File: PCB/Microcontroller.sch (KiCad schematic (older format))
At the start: 9 parts

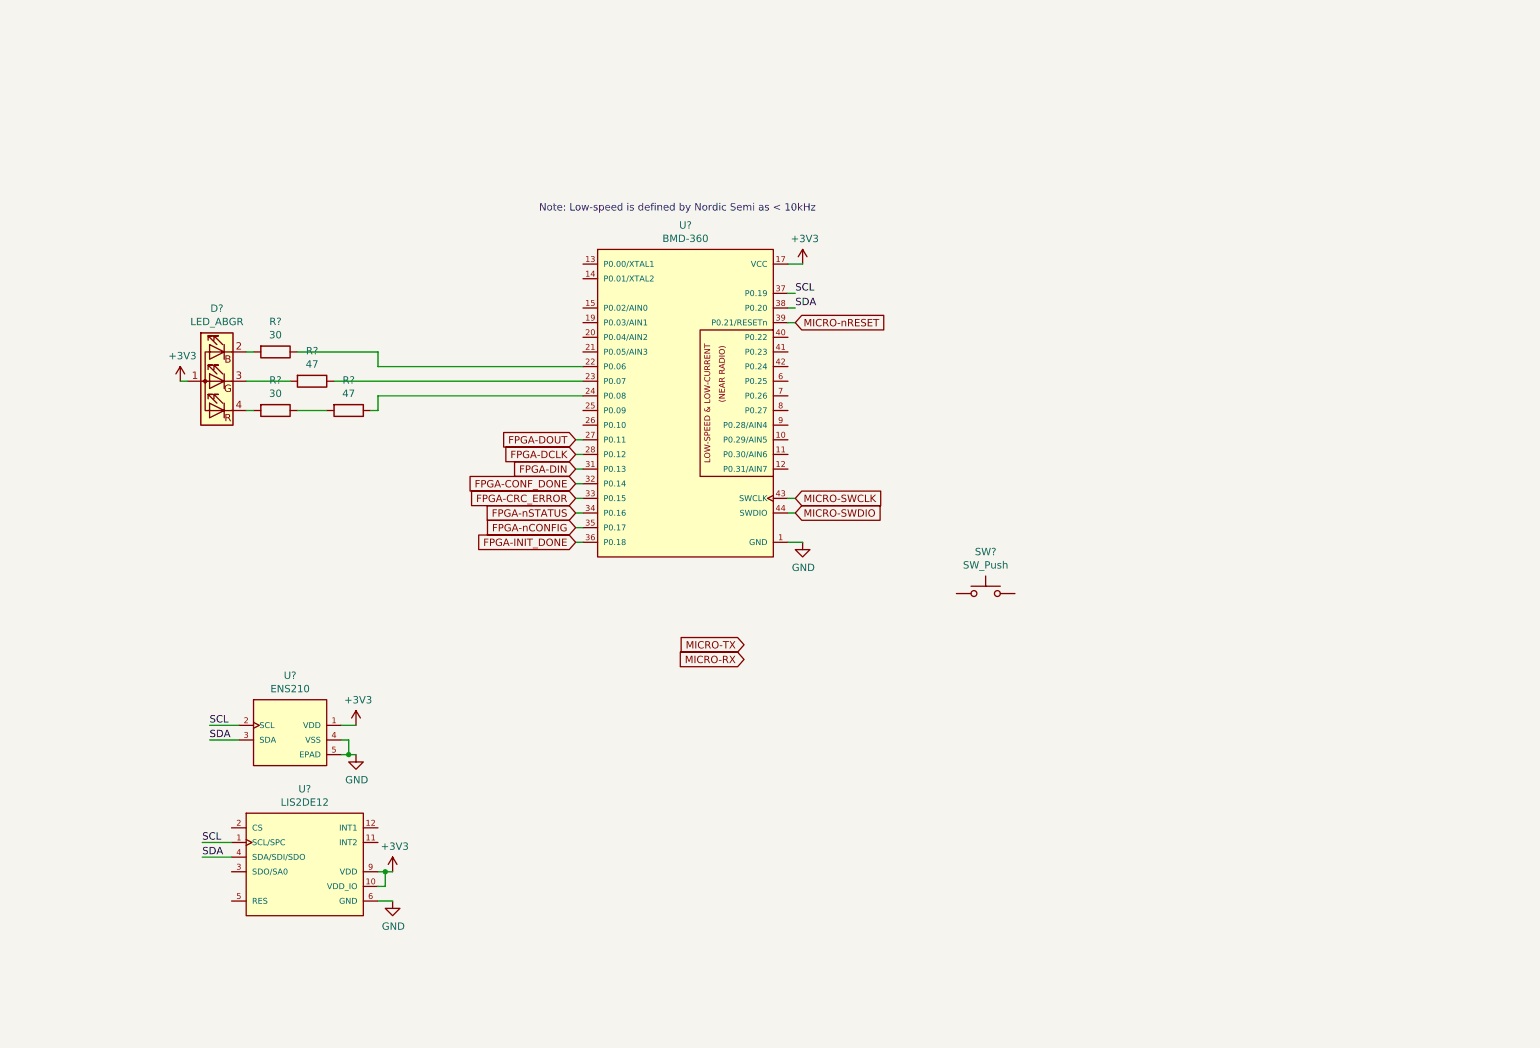
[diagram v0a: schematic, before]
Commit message: Connect push buttons to microcontroller, connect I2C lines, add GPIO links between microcontroller and FPGA
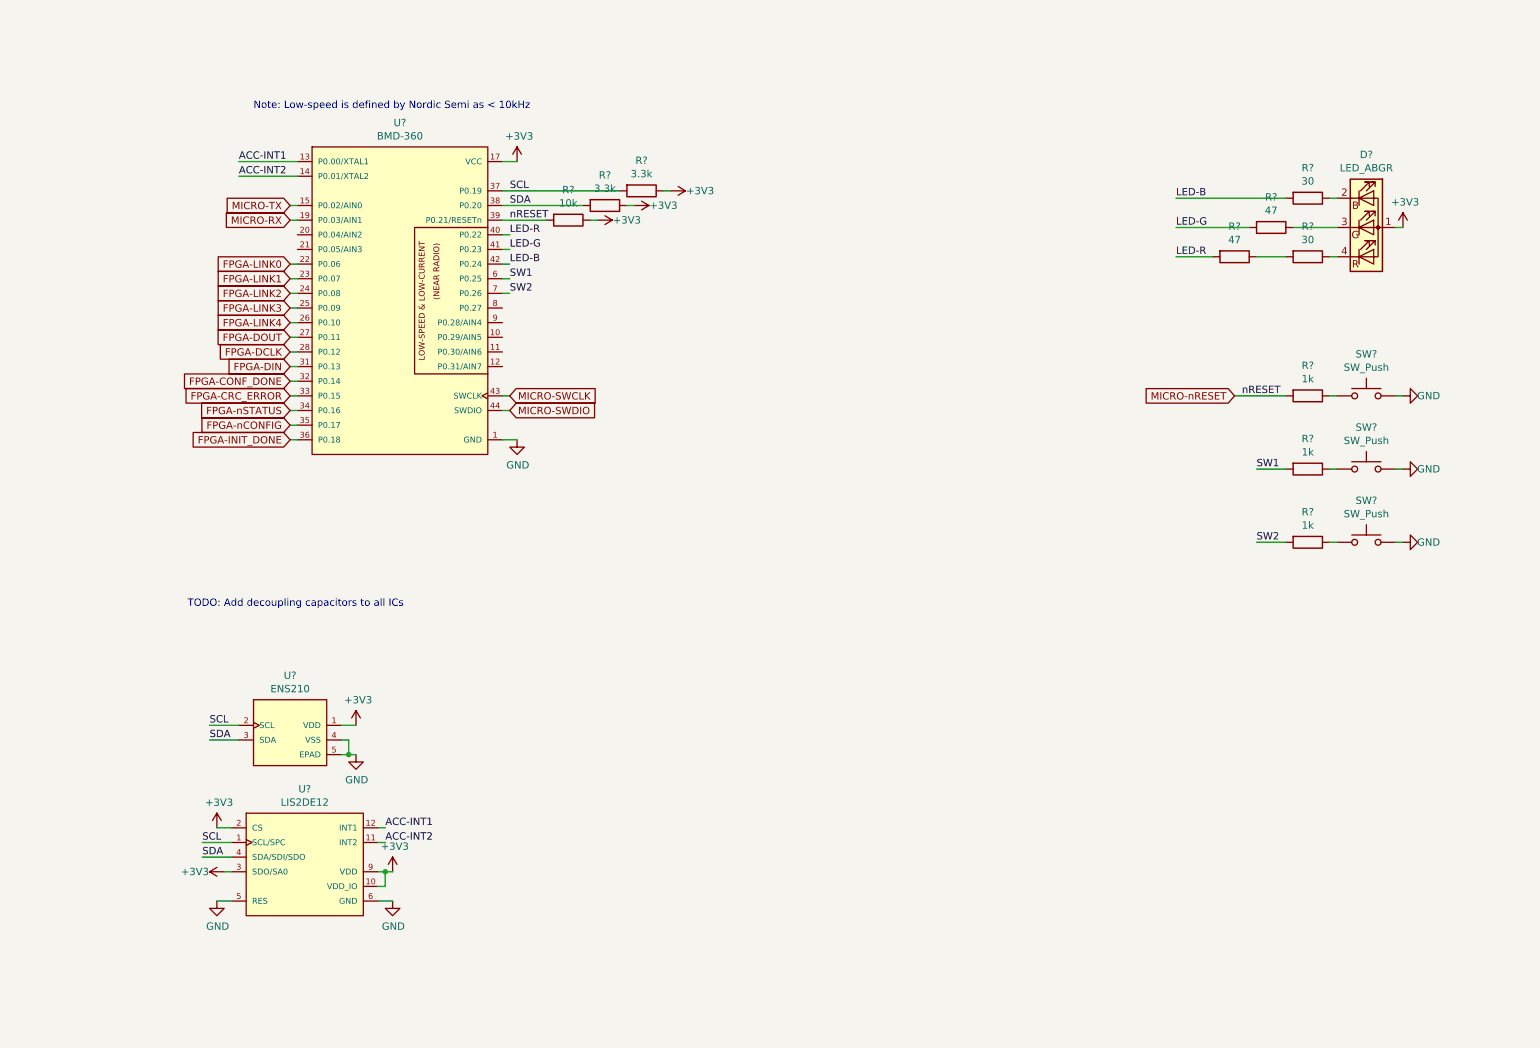
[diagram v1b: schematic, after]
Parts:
- added R?: 10k, Resistors_SMD:R_0603_HandSoldering, symbol Device:R
- added R? (x3): 1k, Resistors_SMD:R_0603_HandSoldering, symbol Device:R
- added R? (x2): 3.3k, Resistors_SMD:R_0603_HandSoldering, symbol Device:R
- added SW? (x2): SW_Push, Parts:PTS645SK43SM, symbol Switch:SW_Push
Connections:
- net +3V3: now also U?.2 (CS), U?.3 (SDO/SA0), R?.1, R?.1, R?.1
- net GND: now also SW?.2, U?.5 (RES), SW?.2, SW?.2
- net MICRO-RX: now also U?.19 (P0.03/AIN1)
- net MICRO-TX: now also U?.15 (P0.02/AIN0)
- net MICRO-nRESET: now also R?.2, R?.2
- net SCL: now also R?.2
- net SDA: now also R?.2
- net at SW?.1: now also R?.1
- net ACC-INT1: now reaches U?.13 (P0.00/XTAL1)
- net ACC-INT1: now also U?.12 (INT1)
- net ACC-INT2: now reaches U?.14 (P0.01/XTAL2)
- net ACC-INT2: now also U?.11 (INT2)
- net at R?.1: now also D?.2 (RK); no longer U?.22 (P0.06)
- net at R?.1: now also D?.3 (GK); no longer U?.23 (P0.07)
- net at R?.1: now also R?.2; no longer U?.24 (P0.08)
- net FPGA-LINK3: now reaches U?.25 (P0.09)
- net FPGA-LINK4: now reaches U?.26 (P0.10)
- net LED-R: now reaches U?.40 (P0.22)
- net LED-R: now also R?.2
- net LED-G: now reaches U?.41 (P0.23)
- net LED-G: now also R?.2
- net LED-B: now reaches U?.42 (P0.24)
- net LED-B: now also R?.2
- net SW1: now reaches U?.6 (P0.25)
- net SW1: now also R?.2
- net SW2: now reaches U?.7 (P0.26)
- net SW2: now also R?.2
- net at D?.4 (BK): now also R?.1; no longer R?.2
- new net: R?.1, SW?.1 (x2)
- new net FPGA-LINK0: U?.22 (P0.06)
- new net FPGA-LINK1: U?.23 (P0.07)
- new net FPGA-LINK2: U?.24 (P0.08)
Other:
- note added: "TODO: Add decoupling capacitors to all ICs"
- moved on the sheet: D?, R?, SW?, U?

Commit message: Added low-noise supply rails, changed 100nF capacitors to 0603 footprint, fixed ENS210 footprint, added decoupling capacitors to microcontroller
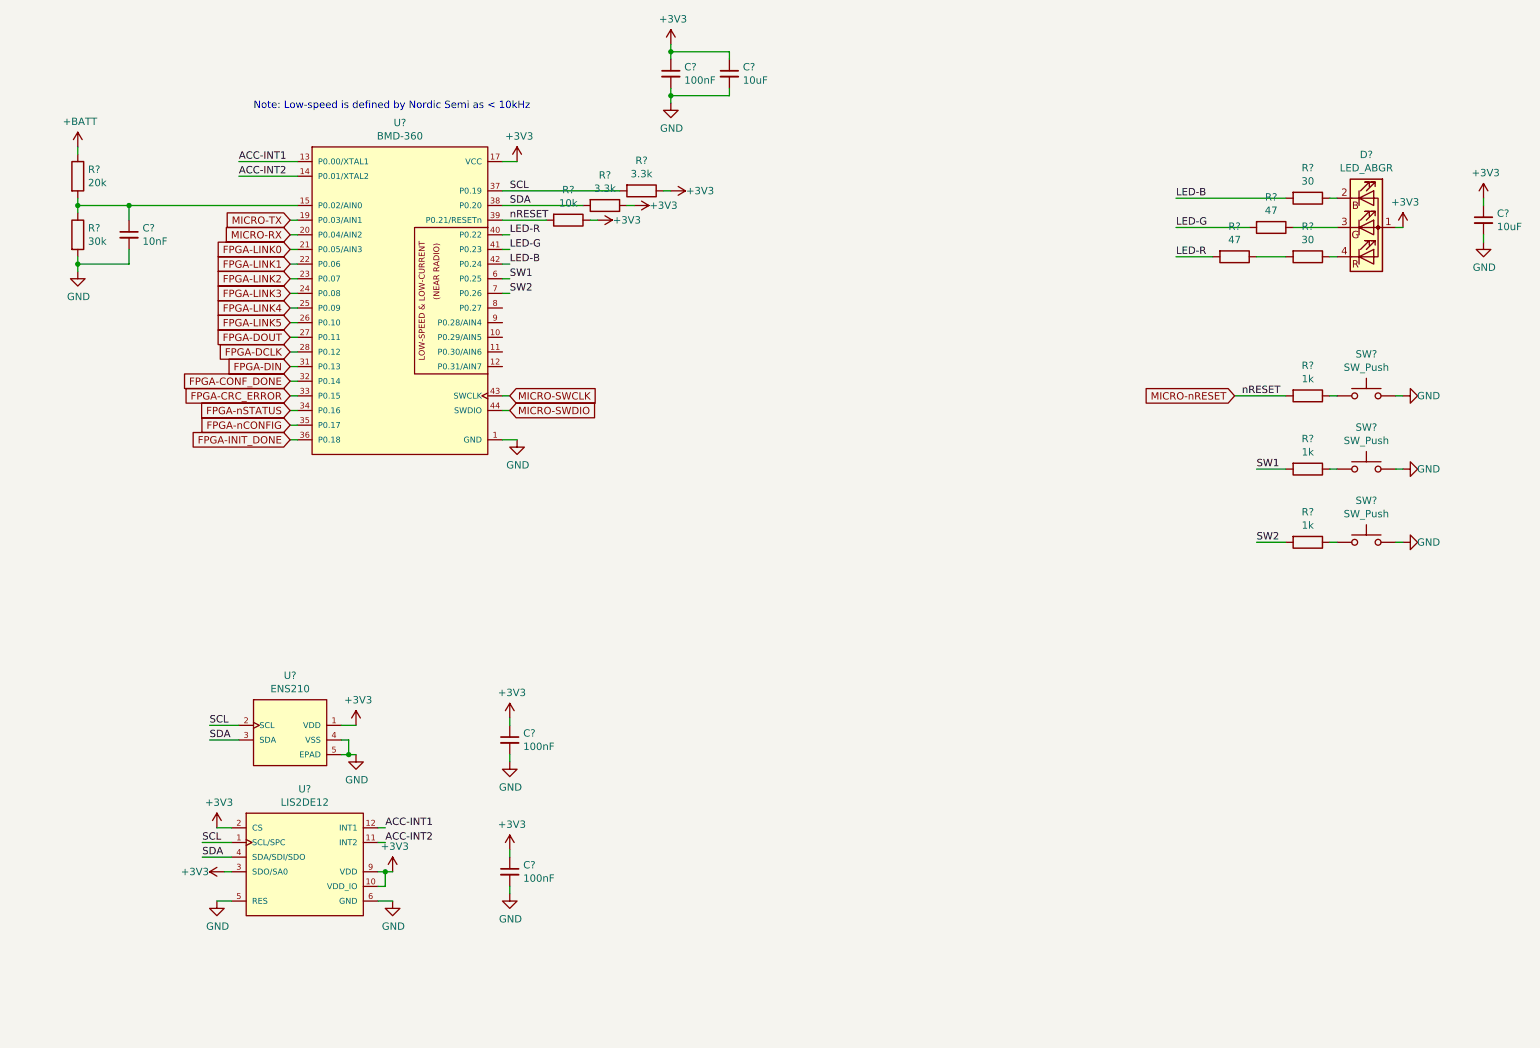
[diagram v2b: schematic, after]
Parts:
- added C? (x3): 100nF, Capacitors_SMD:C_0603_HandSoldering, symbol Device:C_Small
- added C? (x2): 10uF, Capacitors_SMD:C_0805_HandSoldering, symbol Device:C_Small
- added C?: 10nF, Capacitors_SMD:C_0603_HandSoldering, symbol Device:C_Small
- added R?: 20k, Resistors_SMD:R_0603_HandSoldering, symbol Device:R
- added R?: 30k, Resistors_SMD:R_0603_HandSoldering, symbol Device:R
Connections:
- net +3V3: now also C?.1, C?.1, C?.1, C?.1, C?.1
- net FPGA-LINK0: now also U?.21 (P0.05/AIN3); no longer U?.22 (P0.06)
- net FPGA-LINK1: now also U?.22 (P0.06); no longer U?.23 (P0.07)
- net FPGA-LINK2: now also U?.23 (P0.07); no longer U?.24 (P0.08)
- net FPGA-LINK3: now also U?.24 (P0.08); no longer U?.25 (P0.09)
- net FPGA-LINK4: now also U?.25 (P0.09); no longer U?.26 (P0.10)
- net GND: now also C?.2, C?.2, C?.2, C?.2, C?.2, C?.2, R?.2
- net MICRO-RX: now also U?.20 (P0.04/AIN2); no longer U?.19 (P0.03/AIN1)
- net MICRO-TX: now also U?.19 (P0.03/AIN1); no longer U?.15 (P0.02/AIN0)
- new net: C?.1, R?.1, R?.2, U?.15 (P0.02/AIN0)
- new net +BATT: R?.1
- new net FPGA-LINK5: U?.26 (P0.10)
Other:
- note removed: "TODO: Add decoupling capacitors to all ICs"

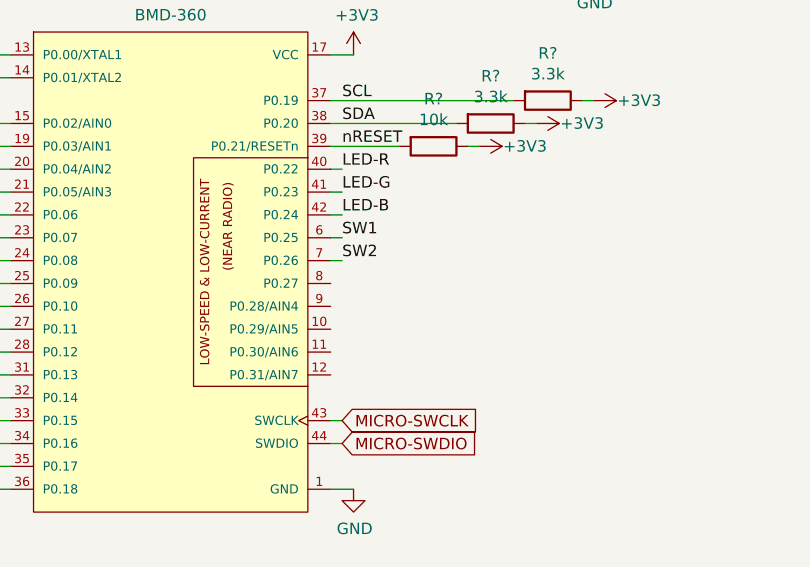
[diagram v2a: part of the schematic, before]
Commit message: Add LMR62421 regulator and inductor to library, draw schematic for 12V supply, add HV-ENABLE pin to microcontroller
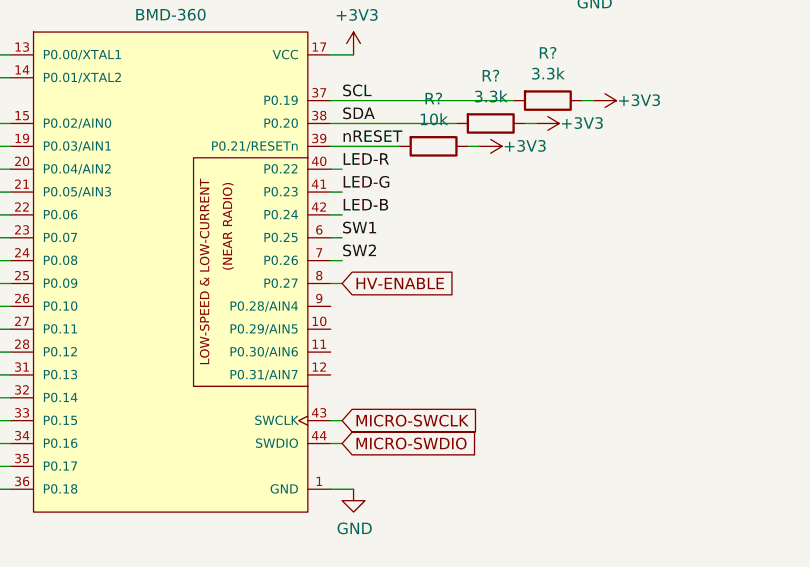
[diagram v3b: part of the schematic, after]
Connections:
- net HV-ENABLE: now reaches U?.8 (P0.27)
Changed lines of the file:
@@
 Wire Wire Line
 	10650 2200 10650 2250
+Text GLabel 4000 2700 2    50   Input ~ 0
+HV-ENABLE
+Wire Wire Line
+	3950 2700 4000 2700
 $EndSCHEMATC
